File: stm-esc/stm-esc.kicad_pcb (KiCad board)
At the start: 2 copper layers, 90 x 90 mm, 48 parts, among them J1 Conn_01x06, J10 Conn_01x02, J11 AOUT, J12 Conn_01x02, J13 CONN_01X01, J14 CONN_01X01, J15 BOUT, J16 COUT, J3 Conn_01x06, J4 Conn_01x03, J5 Conn_01x02, J6 Conn_01x06, J7 Conn_01x04, J8 Conn_01x04, J9 Conn_01x06, Q1 FDMS86350, Q2 FDMS86350, Q3 FDMS86350, Q4 FDMS86350, Q5 FDMS86350, Q6 FDMS86350, U1 L7805, U2 APE8865N-33-HF-3, U3 STM32F0XX-QFP48, U4 IR2103, U5 IR2103, U6 IR2103

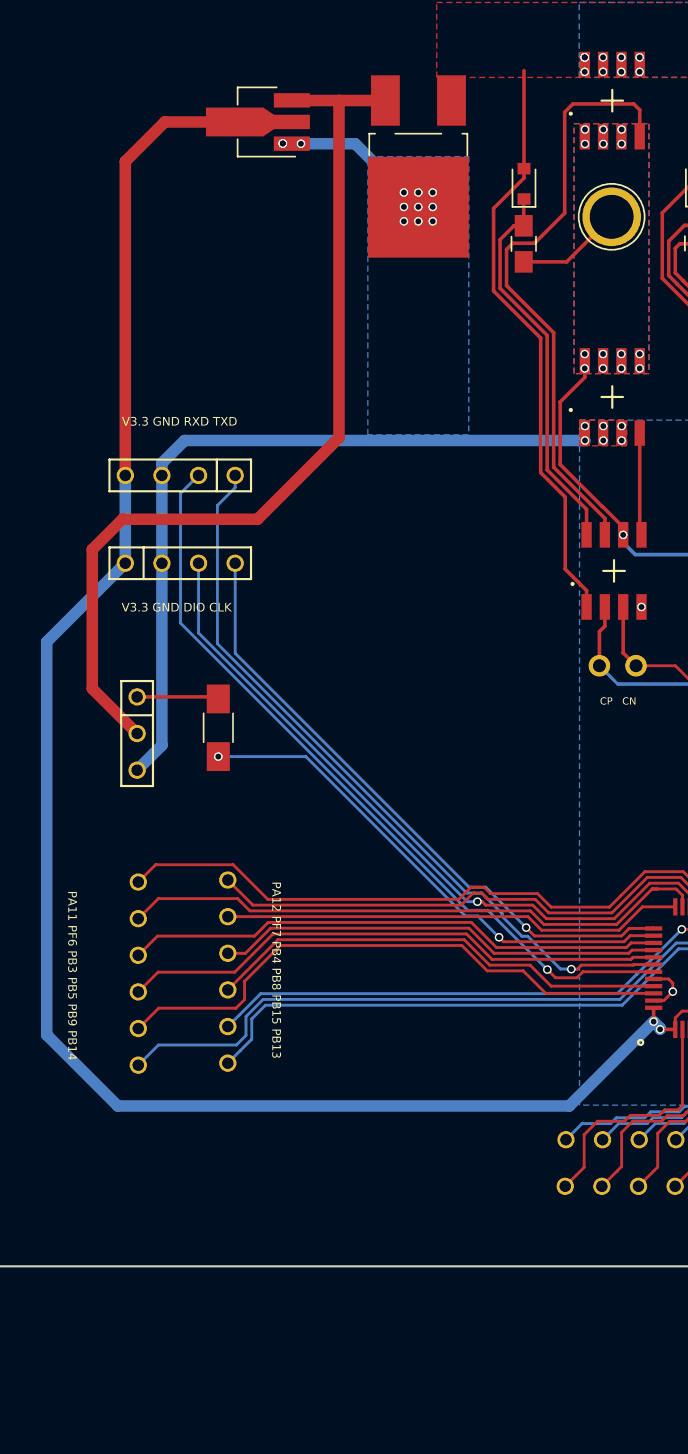
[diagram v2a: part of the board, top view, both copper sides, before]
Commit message: correct pin define for regular v3.3
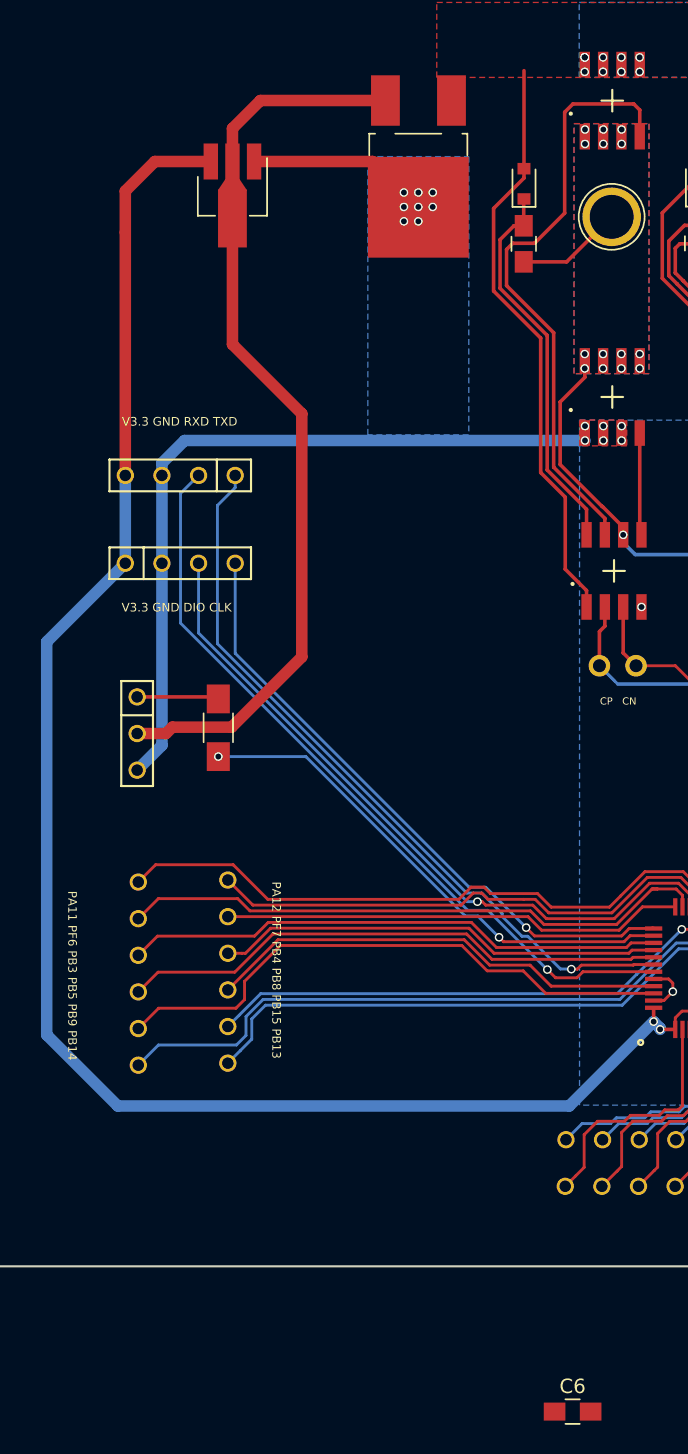
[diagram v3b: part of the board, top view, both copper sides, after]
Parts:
- added C6: C, Capacitors_SMD:C_0805_HandSoldering, F.Cu at (65.0, 120.1)
- moved U2 5.18 mm to (41.4, 35.4), turned to 270 degrees
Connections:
- U2 pad 2: +3V3 -> +5V
- U2 pad 3: +5V -> +3V3
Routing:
- net +5V: track 64.3 -> 59.7 mm
- net +3V3: track 144.6 -> 140.6 mm
- net GND: vias 38 -> 34
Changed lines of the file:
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@@
 (kicad_pcb (version 4) (host pcbnew 4.0.7)
   (general
-    (links 159)
-    (no_connects 4)
+    (links 161)
+    (no_connects 8)
     (area 19.924999 19.924999 110.075001 110.075001)
     (thickness 1.6)
     (drawings 13)
-    (tracks 799)
+    (tracks 794)
     (zones 0)
-    (modules 48)
+    (modules 49)
     (nets 58)
   )
@@
   )
   (setup
-    (last_trace_width 0.2)
+    (last_trace_width 0.8)
     (user_trace_width 0.2)
     (user_trace_width 0.8)
@@
   )
   (module TO_SOT_Packages_SMD:SOT-89-3_Handsoldering (layer F.Cu)
-    (at 43.55 30.64 180)
+    (at 41.41 35.36 270)
     (descr "SOT-89-3 Handsoldering")
     (tags "SOT-89-3 Handsoldering")
     (attr smd)
-    (fp_text reference U2 (at 0.45 -3.3 180) (layer F.SilkS) hide
-      (effects (font (size 1 1) (thickness 0.15)))
-    )
-    (fp_text value APE8865N-33-HF-3 (at 0.5 3.15 180) (layer F.Fab) hide
-      (effects (font (size 1 1) (thickness 0.15)))
-    )
-    (fp_text user %R (at 0.38 0 270) (layer F.Fab)
+    (fp_text reference U2 (at 0.45 -3.3 270) (layer F.SilkS) hide
+      (effects (font (size 1 1) (thickness 0.15)))
+    )
+    (fp_text value APE8865N-33-HF-3 (at 0.5 3.15 270) (layer F.Fab) hide
+      (effects (font (size 1 1) (thickness 0.15)))
+    )
+    (fp_text user %R (at 0.38 0 360) (layer F.Fab)
       (effects (font (size 0.6 0.6) (thickness 0.09)))
     )
@@
     (fp_line (start -0.92 2.3) (end -0.92 -1.51) (layer F.Fab) (width 0.1))
     (fp_line (start -0.13 -2.3) (end 1.68 -2.3) (layer F.Fab) (width 0.1))
-    (pad 1 smd rect (at -1.98 -1.5 90) (size 1 2.5) (layers F.Cu F.Paste F.Mask)
-      (net 1 GND))
-    (pad 2 smd rect (at -1.98 0 90) (size 1 2.5) (layers F.Cu F.Paste F.Mask)
+    (pad 1 smd rect (at -1.98 -1.5 180) (size 1 2.5) (layers F.Cu F.Paste F.Mask)
+      (net 1 GND))
+    (pad 2 smd rect (at -1.98 0 180) (size 1 2.5) (layers F.Cu F.Paste F.Mask)
+      (net 12 +5V))
+    (pad 3 smd rect (at -1.98 1.5 180) (size 1 2.5) (layers F.Cu F.Paste F.Mask)
       (net 2 +3V3))
-    (pad 3 smd rect (at -1.98 1.5 90) (size 1 2.5) (layers F.Cu F.Paste F.Mask)
+    (pad 2 smd rect (at 1.98 0 180) (size 2 4) (layers F.Cu F.Paste F.Mask)
       (net 12 +5V))
-    (pad 2 smd rect (at 1.98 0 90) (size 2 4) (layers F.Cu F.Paste F.Mask)
-      (net 2 +3V3))
-    (pad 2 smd trapezoid (at -0.37 0 270) (size 1.5 0.75) (rect_delta 0 0.5 ) (layers F.Cu F.Paste F.Mask)
-      (net 2 +3V3))
+    (pad 2 smd trapezoid (at -0.37 0) (size 1.5 0.75) (rect_delta 0 0.5 ) (layers F.Cu F.Paste F.Mask)
+      (net 12 +5V))
     (model ${KISYS3DMOD}/TO_SOT_Packages_SMD.3dshapes/SOT-89-3.wrl
       (at (xyz 0 0 0))
@@
     )
   )
+  (module Capacitors_SMD:C_0805_HandSoldering (layer F.Cu)
+    (at 65 120.075001)
+    (descr "Capacitor SMD 0805, hand soldering")
+    (tags "capacitor 0805")
+    (attr smd)
+    (fp_text reference C6 (at 0 -1.75) (layer F.SilkS)
+      (effects (font (size 1 1) (thickness 0.15)))
+    )
+    (fp_text value C (at 0 1.75) (layer F.Fab)
+      (effects (font (size 1 1) (thickness 0.15)))
+    )
+    (fp_text user %R (at 0 -1.75) (layer F.Fab)
+      (effects (font (size 1 1) (thickness 0.15)))
+    )
+    (fp_line (start -1 0.62) (end -1 -0.62) (layer F.Fab) (width 0.1))
+    (fp_line (start 1 0.62) (end -1 0.62) (layer F.Fab) (width 0.1))
+    (fp_line (start 1 -0.62) (end 1 0.62) (layer F.Fab) (width 0.1))
+    (fp_line (start -1 -0.62) (end 1 -0.62) (layer F.Fab) (width 0.1))
+    (fp_line (start 0.5 -0.85) (end -0.5 -0.85) (layer F.SilkS) (width 0.12))
+    (fp_line (start -0.5 0.85) (end 0.5 0.85) (layer F.SilkS) (width 0.12))
+    (fp_line (start -2.25 -0.88) (end 2.25 -0.88) (layer F.CrtYd) (width 0.05))
+    (fp_line (start -2.25 -0.88) (end -2.25 0.87) (layer F.CrtYd) (width 0.05))
+    (fp_line (start 2.25 0.87) (end 2.25 -0.88) (layer F.CrtYd) (width 0.05))
+    (fp_line (start 2.25 0.87) (end -2.25 0.87) (layer F.CrtYd) (width 0.05))
+    (pad 1 smd rect (at -1.25 0) (size 1.5 1.25) (layers F.Cu F.Paste F.Mask)
+      (net 1 GND))
+    (pad 2 smd rect (at 1.25 0) (size 1.5 1.25) (layers F.Cu F.Paste F.Mask)
+      (net 33 /Vsample))
+    (model Capacitors_SMD.3dshapes/C_0805.wrl
+      (at (xyz 0 0 0))
+      (scale (xyz 1 1 1))
+      (rotate (xyz 0 0 0))
+    )
+  )
   (gr_text "AP   AN" (at 91.41 70.71) (layer F.SilkS)
     (effects (font (size 0.5 0.5) (thickness 0.05)))
@@
   (gr_line (start 20 20) (end 20 110) (layer Edge.Cuts) (width 0.15))
   (gr_line (start 20 20) (end 110 20) (layer Edge.Cuts) (width 0.15))
+  (segment (start 42.91 33.38) (end 51.13 33.38) (width 0.8) (layer F.Cu) (net 1))
+  (segment (start 51.13 33.38) (end 54.3 36.55) (width 0.8) (layer F.Cu) (net 1))
   (segment (start 71.95 90.36) (end 71.95 90.95) (width 0.2) (layer F.Cu) (net 1))
   (segment (start 70.62 91.57) (end 71.33 91.57) (width 0.2) (layer F.Cu) (net 1))
@@
   (via (at 81.427514 64.272068) (size 0.6) (drill 0.4) (layers F.Cu B.Cu) (net 1))
   (via (at 69.777514 64.272068) (size 0.6) (drill 0.4) (layers F.Cu B.Cu) (net 1))
-  (segment (start 46.16 32.15) (end 49.92 32.15) (width 0.8) (layer B.Cu) (net 1))
-  (segment (start 49.92 32.15) (end 55.3 37.53) (width 0.8) (layer B.Cu) (net 1))
-  (segment (start 44.9 32.13) (end 46.14 32.13) (width 0.8) (layer B.Cu) (net 1))
-  (segment (start 46.14 32.13) (end 46.16 32.15) (width 0.8) (layer B.Cu) (net 1))
-  (via (at 46.16 32.15) (size 0.6) (drill 0.4) (layers F.Cu B.Cu) (net 1))
-  (via (at 44.9 32.13) (size 0.6) (drill 0.4) (layers F.Cu B.Cu) (net 1))
-  (via (at 44.9 32.13) (size 0.6) (drill 0.4) (layers F.Cu B.Cu) (net 1))
-  (via (at 55.3 37.53) (size 0.6) (drill 0.4) (layers F.Cu B.Cu) (net 1))
   (via (at 54.3 37.53) (size 0.6) (drill 0.4) (layers F.Cu B.Cu) (net 1))
   (via (at 53.3 37.53) (size 0.6) (drill 0.4) (layers F.Cu B.Cu) (net 1))
@@
   (via (at 67.13 51.73) (size 0.6) (drill 0.4) (layers F.Cu B.Cu) (net 1))
   (via (at 65.86 51.73) (size 0.6) (drill 0.4) (layers F.Cu B.Cu) (net 1))
+  (segment (start 33.98 55.15) (end 33.98 38.3) (width 0.8) (layer F.Cu) (net 2) (status 400000))
+  (segment (start 36.03 33.38) (end 39.91 33.38) (width 0.8) (layer F.Cu) (net 2) (status 800000))
+  (segment (start 33.98 35.43) (end 36.03 33.38) (width 0.8) (layer F.Cu) (net 2))
+  (segment (start 33.98 38.3) (end 33.98 35.43) (width 0.8) (layer F.Cu) (net 2))
   (segment (start 70.62 93.03) (end 64.77 98.88) (width 0.8) (layer B.Cu) (net 2))
   (segment (start 64.77 98.88) (end 33.46 98.88) (width 0.8) (layer B.Cu) (net 2))
@@
   (segment (start 28.53 93.95) (end 28.53 66.69) (width 0.8) (layer B.Cu) (net 2))
   (segment (start 33.98 61.24) (end 33.98 55.15) (width 0.8) (layer B.Cu) (net 2))
-  (segment (start 33.98 55.15) (end 33.98 33.38) (width 0.8) (layer F.Cu) (net 2))
-  (segment (start 33.98 33.38) (end 36.72 30.64) (width 0.8) (layer F.Cu) (net 2))
-  (segment (start 36.72 30.64) (end 41.57 30.64) (width 0.8) (layer F.Cu) (net 2))
   (segment (start 76.130001 92.759999) (end 76.130001 92.32) (width 0.2) (layer F.Cu) (net 2))
   (segment (start 76.130001 92.32) (end 76.130001 90.890001) (width 0.2) (layer F.Cu) (net 2))
@@
   (via (at 67.11 26.16) (size 0.6) (drill 0.4) (layers F.Cu B.Cu) (net 11))
   (via (at 65.84 26.16) (size 0.6) (drill 0.4) (layers F.Cu B.Cu) (net 11))
-  (segment (start 52.02 29.15) (end 48.82 29.15) (width 0.8) (layer F.Cu) (net 12))
-  (segment (start 48.82 29.15) (end 45.54 29.15) (width 0.8) (layer F.Cu) (net 12))
-  (segment (start 48.8 52.54) (end 48.8 29.17) (width 0.8) (layer F.Cu) (net 12))
-  (segment (start 48.8 29.17) (end 48.82 29.15) (width 0.8) (layer F.Cu) (net 12))
-  (segment (start 45.54 29.15) (end 45.53 29.14) (width 0.8) (layer F.Cu) (net 12))
-  (segment (start 43.15 58.19) (end 48.8 52.54) (width 0.8) (layer F.Cu) (net 12))
-  (segment (start 33.79 58.19) (end 43.15 58.19) (width 0.8) (layer F.Cu) (net 12))
-  (segment (start 31.69 60.29) (end 33.79 58.19) (width 0.8) (layer F.Cu) (net 12))
-  (segment (start 34.8 73.05) (end 31.69 69.94) (width 0.8) (layer F.Cu) (net 12))
-  (segment (start 31.69 69.94) (end 31.69 60.29) (width 0.8) (layer F.Cu) (net 12))
+  (segment (start 46.22 50.87) (end 41.41 46.06) (width 0.8) (layer F.Cu) (net 12))
+  (segment (start 41.41 46.06) (end 41.41 37.34) (width 0.8) (layer F.Cu) (net 12))
+  (segment (start 46.22 67.740002) (end 46.22 50.87) (width 0.8) (layer F.Cu) (net 12))
+  (segment (start 37.24 72.61) (end 41.350002 72.61) (width 0.8) (layer F.Cu) (net 12))
+  (segment (start 41.350002 72.61) (end 46.22 67.740002) (width 0.8) (layer F.Cu) (net 12))
+  (segment (start 36.8 73.05) (end 37.24 72.61) (width 0.8) (layer F.Cu) (net 12))
+  (segment (start 34.8 73.05) (end 36.8 73.05) (width 0.8) (layer F.Cu) (net 12))
+  (segment (start 41.41 33.38) (end 41.41 31.09) (width 0.8) (layer F.Cu) (net 12) (status 400000))
+  (segment (start 43.35 29.15) (end 52.02 29.15) (width 0.8) (layer F.Cu) (net 12) (status 800000))
+  (segment (start 41.41 31.09) (end 43.35 29.15) (width 0.8) (layer F.Cu) (net 12))
   (segment (start 91.807514 64.272068) (end 91.807514 67.407514) (width 0.25) (layer F.Cu) (net 13))
   (segment (start 91.807514 67.407514) (end 92.75 68.35) (width 0.25) (layer F.Cu) (net 13))

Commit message: working
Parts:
- removed the R2 at (98.1, 92.2)
- removed the R2 at (100.6, 92.2)
- added BT1: Battery_Cell, Battery:BatteryHolder_Keystone_103_1x20mm, F.Cu at (0.00, 0.00)
- added BZ1: Buzzer, Buzzer_Beeper:Buzzer_12x9.5RM7.6, F.Cu at (20.0, 0.00)
- added C7: Cb, Capacitor_SMD:C_0603_1608Metric_Pad1.05x0.95mm_HandSolder, F.Cu at (89.7, 40.9)
- added D4: Dc, Diode_SMD:D_0603_1608Metric_Pad1.05x0.95mm_HandSolder, F.Cu at (79.7, 38.4)
- added D5: Db, Diode_SMD:D_0603_1608Metric_Pad1.05x0.95mm_HandSolder, F.Cu at (90.6, 38.4)
- added J2: Conn_01x06, footprint:conn-6x2.54mm, F.Cu at (120.0, 20.0)
- added Q7: nfet, footprint:SOIC-8, F.Cu at (85.6, 43.4)
- added R13: 1k, Resistor_SMD:R_0603_1608Metric_Pad1.05x0.95mm_HandSolder, F.Cu at (78.9, 78.8)
- added R14: 20k, Resistor_SMD:R_0603_1608Metric_Pad1.05x0.95mm_HandSolder, F.Cu at (82.6, 82.5)
- added R15: 20k, Resistor_SMD:R_0603_1608Metric_Pad1.05x0.95mm_HandSolder, F.Cu at (82.6, 78.8)
- added R2: 1R, Resistor_SMD:R_0805_2012Metric_Pad1.15x1.40mm_HandSolder, F.Cu at (79.3, 75.2)
- C1: footprint Capacitors_SMD:C_1206_HandSoldering -> Capacitor_SMD:C_0603_1608Metric_Pad1.05x0.95mm_HandSolder
- C2: footprint Capacitors_SMD:C_1206_HandSoldering -> Capacitor_SMD:C_0805_2012Metric_Pad1.15x1.40mm_HandSolder
- C3: footprint Capacitors_SMD:C_0805_HandSoldering -> Capacitor_SMD:C_0603_1608Metric
- C4: footprint Capacitors_SMD:C_0805_HandSoldering -> Capacitor_SMD:C_0603_1608Metric_Pad1.05x0.95mm_HandSolder
- C5: value C -> Ca; footprint Capacitors_SMD:C_0805_HandSoldering -> Capacitor_SMD:C_0603_1608Metric_Pad1.05x0.95mm_HandSolder
- C6: value C -> Cc; footprint Capacitors_SMD:C_0805_HandSoldering -> Capacitor_SMD:C_0603_1608Metric_Pad1.05x0.95mm_HandSolder
- D1: footprint Diodes_SMD:D_0805 -> Diode_THT:D_5W_P10.16mm_Horizontal
- D2: value D -> LED; footprint Diodes_SMD:D_0805 -> LED_THT:LED_D4.0mm
- D3: value D -> Da; footprint Diodes_SMD:D_0805 -> Diode_SMD:D_0603_1608Metric_Pad1.05x0.95mm_HandSolder
- J1, J3: footprint my_footprint:conn-6x2.54mm -> footprint:conn-6x2.54mm
- J10: value Conn_01x02 -> Conn_01x03; footprint my_footprint:SIP-2xP2.54mm -> footprint:conn-3x2.54mm
- J11: value AOUT -> Conn_01x02; footprint Connectors:1pin -> footprint:SIP-2xP2.54mm
- J12: footprint my_footprint:SIP-2xP2.54mm -> footprint:SIP-2xP2.54mm
- J13: value CONN_01X01 -> Conn_01x02; footprint Connectors:1pin -> footprint:SIP-2xP2.54mm
- J14: value CONN_01X01 -> Conn_01x01; footprint Connectors:1pin -> footprint:HOLE-R1.5MM
- J15: value BOUT -> Conn_01x01; footprint Connectors:1pin -> footprint:HOLE-R1.5MM
- J16: value COUT -> Conn_01x01; footprint Connectors:1pin -> footprint:HOLE-R1.5MM
- J4: value Conn_01x03 -> Conn_01x06; footprint my_footprint:conn-3x2.54mm -> footprint:conn-6x2.54mm
- J5: value Conn_01x02 -> Conn_01x01; footprint my_footprint:SIP-2xP2.54mm -> Connector_Pin:Pin_D1.3mm_L10.0mm_W3.5mm_Flat
- J6: value Conn_01x06 -> Conn_01x04; footprint my_footprint:conn-6x2.54mm -> Connector_PinSocket_2.54mm:PinSocket_1x04_P2.54mm_Vertical
- J7: footprint my_footprint:conn-4x2.54mm -> Connector_PinSocket_2.54mm:PinSocket_1x04_P2.54mm_Vertical
- J8: value Conn_01x04 -> Conn_01x01; footprint my_footprint:conn-4x2.54mm -> footprint:HOLE-R1.5MM
- J9: value Conn_01x06 -> Conn_01x01; footprint my_footprint:conn-6x2.54mm -> footprint:HOLE-R1.5MM
- Q1: value FDMS86350 -> 2N7002; footprint my_footprint:SOIC-8 -> Package_TO_SOT_SMD:SOT-23
- Q2, Q3, Q4, Q5, Q6: value FDMS86350 -> nfet; footprint my_footprint:SOIC-8 -> footprint:SOIC-8
- R1: value R -> 1k; footprint Resistors_SMD:R_0805_HandSoldering -> Resistor_SMD:R_0603_1608Metric_Pad1.05x0.95mm_HandSolder
- R10, R12, R8: value 20K -> 20k; footprint Resistors_SMD:R_0603_HandSoldering -> Resistor_SMD:R_0603_1608Metric_Pad1.05x0.95mm_HandSolder
- R11, R7, R9: value 20K -> 3k; footprint Resistors_SMD:R_0603_HandSoldering -> Resistor_SMD:R_0603_1608Metric_Pad1.05x0.95mm_HandSolder
- R3: value 3K -> 1K; footprint Resistors_SMD:R_0603_HandSoldering -> Resistor_THT:R_Axial_DIN0204_L3.6mm_D1.6mm_P7.62mm_Horizontal
- R4, R5: value 3K -> 2K; footprint Resistors_SMD:R_0603_HandSoldering -> Resistor_SMD:R_0805_2012Metric_Pad1.15x1.40mm_HandSolder
- R6: value 1K -> 20k; footprint Resistors_SMD:R_0603_HandSoldering -> Resistor_SMD:R_0603_1608Metric_Pad1.05x0.95mm_HandSolder
- U1: value L7805 -> STM32F051C8Tx; footprint TO_SOT_Packages_SMD:TO-252-2_Rectifier -> Package_QFP:LQFP-48_7x7mm_P0.5mm
- U2: value APE8865N-33-HF-3 -> KA78M05_TO252; footprint TO_SOT_Packages_SMD:SOT-89-3_Handsoldering -> Package_TO_SOT_SMD:TO-252-2
- U3: value STM32F0XX-QFP48 -> REGULAR-7133-1; footprint my_footprint:QFP_48_P0.5_W0.3 -> Package_TO_SOT_SMD:SOT-89-3_Handsoldering
- U4, U5, U6: footprint my_footprint:SOIC-8 -> footprint:SOIC-8
- moved J4 136.0 mm to (160.0, 20.0), turned to 0 degrees
- moved J3 109.2 mm to (140.0, 20.0), turned to 0 degrees
- moved J1 89.1 mm to (100.3, 17.2)
- moved Q1 88.9 mm to (4.61, 50.0), turned to 0 degrees
- moved D1 86.6 mm to (0.00, 20.0), turned to 0 degrees
- moved J9 84.3 mm to (106.9, 45.9), turned to 0 degrees
- moved R1 81.0 mm to (20.0, 80.0), turned to 0 degrees
- moved C6 80.3 mm to (78.8, 40.9), turned to 180 degrees
- moved J8 78.5 mm to (106.9, 24.1)
- moved J5 73.8 mm to (0.00, 40.0)
- moved J10 60.3 mm to (93.3, 8.12)
- moved D2 55.7 mm to (20.0, 20.0), turned to 0 degrees
- moved C4 54.3 mm to (82.2, 92.7), turned to 180 degrees
- moved J6 53.9 mm to (20.0, 40.0), turned to 0 degrees
- moved U1 52.6 mm to (88.5, 73.7), turned to 0 degrees
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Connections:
- C1 pad 1: +3V3 -> GND
- C1 pad 2: GND -> /Vdda
- C2 pad 1: /RCP -> GND
- C2 pad 2: Net-(C2-Pad2) -> +3V3
- C3 pad 2: AOUT -> RCP
- C4 pad 1: Net-(C4-Pad1) -> V_SAMPLE
- C4 pad 2: BOUT -> GND
- C5 pad 2: COUT -> /bridge a/AOUT
- C6 pad 1: GND -> Net-(C6-Pad1)
- C6 pad 2: /Vsample -> /bridge c/COUT
- D1 pad 1: Net-(C3-Pad1) -> Net-(BT1-Pad1)
- D1 pad 2: VCC -> +3V3
- D2 pad 1: Net-(C4-Pad1) -> GND
- D2 pad 2: VCC -> Net-(D2-Pad2)
- J1 pad 1: /PB12 -> /PB5
- J1 pad 2: /PB11 -> /PB4
- J1 pad 3: /PB10 -> /PB3
- J1 pad 5: /PA3 -> /PC15
- J1 pad 6: /PA2 -> /PC14
- J10 pad 1: AP -> Net-(C3-Pad1)
- J10 pad 2: AN -> +5V
- J11 pad 1: AOUT -> CN
- J12 pad 1: BP -> BN
- J12 pad 2: BN -> BP
- J13 pad 1: VCC -> AN
- J14 pad 1: GND -> /bridge a/AOUT
- J15 pad 1: BOUT -> /bridge c/COUT
- J16 pad 1: COUT -> /bridge b/BOUT
- J3 pad 1: /NRST -> GND
- J3 pad 2: /PF1 -> /PA3
- J3 pad 3: /PF0 -> /PA11
- J3 pad 4: /PC15 -> /PA12
- J3 pad 5: /PC14 -> /PB15
- J3 pad 6: /PC13 -> /PB14
- J4 pad 1: Net-(C2-Pad2) -> /PB13
- J4 pad 2: +5V -> /PB12
- J4 pad 3: GND -> /PB11
- J5 pad 1: CP -> Net-(J5-Pad1)
- J6 pad 1: PB13 -> +3V3
- J6 pad 2: PB15 -> GND
- J6 pad 3: PB8 -> SWCLK
- J6 pad 4: PB4 -> SWDIO
- J7 pad 1: /TXD -> +3V3
- J7 pad 2: /RXD -> GND
- J7 pad 3: GND -> RXD
- J7 pad 4: +3V3 -> TXD
- J8 pad 1: +3V3 -> VCC
- J9 pad 1: PB14 -> GND
- Q1 pad 1: AOUT -> Net-(J5-Pad1)
- Q1 pad 2: AOUT -> GND
- Q1 pad 3: AOUT -> Net-(BZ1-Pad2)
- Q2 pad 1: GND -> /bridge a/AOUT
- Q2 pad 2: GND -> /bridge a/AOUT
- Q2 pad 3: GND -> /bridge a/AOUT
- Q2 pad 5: AOUT -> VCC
- Q2 pad 6: AOUT -> VCC
- Q2 pad 7: AOUT -> VCC
- Q2 pad 8: AOUT -> VCC
- Q3 pad 1: BOUT -> GND
- Q3 pad 2: BOUT -> GND
- Q3 pad 3: BOUT -> GND
- Q3 pad 5: VCC -> /bridge a/AOUT
- Q3 pad 6: VCC -> /bridge a/AOUT
- Q3 pad 7: VCC -> /bridge a/AOUT
- Q3 pad 8: VCC -> /bridge a/AOUT
- Q4 pad 1: GND -> /bridge c/COUT
- Q4 pad 2: GND -> /bridge c/COUT
- Q4 pad 3: GND -> /bridge c/COUT
- Q4 pad 5: BOUT -> VCC
- Q4 pad 6: BOUT -> VCC
- Q4 pad 7: BOUT -> VCC
- Q4 pad 8: BOUT -> VCC
- Q5 pad 1: COUT -> GND
- Q5 pad 2: COUT -> GND
- Q5 pad 3: COUT -> GND
- Q5 pad 5: VCC -> /bridge c/COUT
- Q5 pad 6: VCC -> /bridge c/COUT
- Q5 pad 7: VCC -> /bridge c/COUT
- Q5 pad 8: VCC -> /bridge c/COUT
- Q6 pad 1: GND -> /bridge b/BOUT
- Q6 pad 2: GND -> /bridge b/BOUT
- Q6 pad 3: GND -> /bridge b/BOUT
- Q6 pad 5: COUT -> VCC
- Q6 pad 6: COUT -> VCC
- Q6 pad 7: COUT -> VCC
- Q6 pad 8: COUT -> VCC
- R1 pad 1: /Vsample -> Net-(R1-Pad1)
- R1 pad 2: VCC -> +3V3
- R10 pad 1: Fabc -> /bridge a/AOUT
- R10 pad 2: COUT -> Fa
- R11 pad 1: Fabc -> Fa
- R11 pad 2: BOUT -> GND
- R12 pad 1: Fabc -> /bridge a/AOUT
- R12 pad 2: AOUT -> Fabc
- R3 pad 1: GND -> Net-(D2-Pad2)
- R3 pad 2: Fc -> Net-(R3-Pad2)
- R4 pad 1: GND -> VCC
- R4 pad 2: Fb -> V_SAMPLE
- R5 pad 1: GND -> V_SAMPLE
- R5 pad 2: Fa -> GND
- R6 pad 1: GND -> /bridge c/COUT
- R6 pad 2: Fabc -> Fc
- R7 pad 2: COUT -> GND
- R8 pad 1: Fb -> /bridge b/BOUT
- R8 pad 2: BOUT -> Fb
- R9 pad 1: Fa -> Fb
- R9 pad 2: AOUT -> GND
- U1 pad 1: VCC -> Net-(BT1-Pad1)
- U1 pad 2: GND -> /PC13
- U1 pad 3: +5V -> /PC14
- U2 pad 1: GND -> VCC
- U2 pad 2: +5V -> GND
- U2 pad 3: +3V3 -> +5V
- U3 pad 1: +3V3 -> GND
- U3 pad 2: /PC13 -> +5V
- U3 pad 3: /PC14 -> +3V3
- U4 pad 5: Net-(Q2-Pad4) -> Net-(Q3-Pad4)
- U4 pad 6: AOUT -> /bridge a/AOUT
- U4 pad 7: Net-(Q1-Pad4) -> Net-(Q2-Pad4)
- U4 pad 8: Net-(C3-Pad1) -> Net-(C5-Pad1)
- U5 pad 2: BP -> CP
- U5 pad 3: BN -> CN
- U5 pad 5: Net-(Q4-Pad4) -> Net-(Q5-Pad4)
- U5 pad 6: BOUT -> /bridge c/COUT
- U5 pad 7: Net-(Q3-Pad4) -> Net-(Q4-Pad4)
- U5 pad 8: Net-(C4-Pad1) -> Net-(C6-Pad1)
- U6 pad 2: CP -> BP
- U6 pad 3: CN -> BN
- U6 pad 5: Net-(Q6-Pad4) -> Net-(Q7-Pad4)
- U6 pad 6: COUT -> /bridge b/BOUT
- U6 pad 7: Net-(Q5-Pad4) -> Net-(Q6-Pad4)
- U6 pad 8: Net-(C5-Pad1) -> Net-(C7-Pad1)
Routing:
- net +3V3: track 140.6 -> 21.8 mm, vias 2 -> 0
- net COUT: track 93.3 -> 0.00 mm, vias 16 -> 0
- net /bridge c/COUT: track 0.00 -> 73.0 mm
- net BOUT: track 68.7 -> 0.00 mm, vias 16 -> 0
- net AOUT: track 63.9 -> 0.00 mm, vias 14 -> 0
- net /bridge b/BOUT: track 0.00 -> 62.7 mm
- net GND: track 97.4 -> 35.3 mm, vias 34 -> 1
- net /RXD: track 53.9 -> 0.00 mm, vias 1 -> 0
- net /bridge a/AOUT: track 0.00 -> 52.4 mm
- net /TXD: track 52.0 -> 0.00 mm, vias 1 -> 0
- net /SWDIO: track 49.3 -> 0.00 mm, vias 1 -> 0
- net PB14: track 47.9 -> 0.00 mm, vias 1 -> 0
- net +5V: track 59.7 -> 13.6 mm
- net VCC: track 188.5 -> 143.2 mm, vias 25 -> 5
- net PA11: track 44.3 -> 0.00 mm
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- added copper zone on B.Cu, net /bridge a/AOUT
- added copper zone on F.Cu, net /bridge a/AOUT
- added copper zone on B.Cu, net /bridge b/BOUT
- added copper zone on F.Cu, net /bridge b/BOUT
- added copper zone on B.Cu, net /bridge c/COUT
- added copper zone on F.Cu, net /bridge c/COUT
- removed copper zone on B.Cu, net AOUT
- removed copper zone on F.Cu, net AOUT
- removed copper zone on B.Cu, net BOUT
- removed copper zone on F.Cu, net BOUT
- removed copper zone on B.Cu, net COUT
- removed copper zone on F.Cu, net COUT
- removed copper zone on B.Cu, net VCC
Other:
- net class Default: via_dia 0.6 -> 0.8
- net class power removed
- net class power33 removed
- rule pad_to_mask_clearance: 0.2 -> 0
- rule via_min_drill: 0.3 -> 0
- rule via_min_size: 0.4 -> 0.2
- board text removed: "AP AN"
- board text removed: "BP BN"
- board text removed: "CP CN"
- board text removed: "PA11 PF6 PB3 PB5 PB9 PB14"
- board text removed: "PA12 PF7 PB4 PB8 PB15 PB13"
- board text removed: "PB12 PB11 PB10 PB2 PA3 PA2"
- board text removed: "PC12 PC14 PC15 PF0 PF1 NRST"
- board text removed: "V3.3 GND DIO CLK"
- board text removed: "V3.3 GND RXD TXD"

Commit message: 定板打样，单片机的退偶电容完整，数字电源和模拟电源隔离
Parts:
- added REF**: KiCad-Logo2_6mm_SilkScreen, Symbol:KiCad-Logo2_6mm_SilkScreen, F.Cu at (52.9, 105.5)
- J1: value Conn_01x06 -> A3 A2 B2 B10 F6 A12
- J11: value Conn_01x02 -> CP CN
- J12: value Conn_01x02 -> BP BN
- J13: value Conn_01x02 -> AP AN
- J2: value Conn_01x06 -> GND B12 B13 B14 B15 A11
- J6: value Conn_01x04 -> DIO CLK G 3.3
- J7: value Conn_01x04 -> TXD RXD G 3.3
- moved J4 137.3 mm to (32.6, 71.3), turned to 270 degrees
- moved J3 123.2 mm to (27.9, 71.2), turned to 270 degrees
- moved D2 111.7 mm to (107.0, 90.1), turned to 180 degrees
- moved BZ1 99.0 mm to (27.4, 98.7), turned to 270 degrees
- moved J7 93.3 mm to (106.4, 56.3)
- moved J6 92.1 mm to (106.4, 71.7)
- moved J1 91.2 mm to (82.0, 106.5), turned to 180 degrees
- moved J2 89.0 mm to (99.0, 106.5), turned to 180 degrees
- moved J10 83.6 mm to (23.8, 54.5), turned to 270 degrees
- moved C3 74.1 mm to (27.2, 52.0)
- moved D1 72.5 mm to (59.3, 61.8)
- moved J5 70.1 mm to (37.8, 99.0)
- moved Q1 64.8 mm to (36.8, 106.3), turned to 180 degrees
- moved R1 59.1 mm to (78.6, 72.4), turned to 180 degrees
- moved R3 52.6 mm to (101.8, 81.8), turned to 180 degrees
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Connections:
- J1 pad 1: /PB5 -> /PA12
- J1 pad 2: /PB4 -> /PF6
- J1 pad 3: /PB3 -> /PB10
- J1 pad 5: /PC15 -> /PA2
- J1 pad 6: /PC14 -> /PA3
- J2 pad 1: /PC13 -> /PA11
- J2 pad 2: /PF7 -> /PB15
- J2 pad 3: /PF6 -> /PB14
- J2 pad 4: /PF1 -> /PB13
- J2 pad 5: /PF0 -> /PB12
- J3 pad 2: /PA3 -> /PB5
- J3 pad 3: /PA11 -> /PB3
- J3 pad 4: /PA12 -> /PF7
- J3 pad 5: /PB15 -> /PC14
- J3 pad 6: /PB14 -> /PF0
- J4 pad 1: /PB13 -> /PB8
- J4 pad 2: /PB12 -> /PB9
- J4 pad 3: /PB11 -> /PB4
- J4 pad 4: /PB10 -> /PC13
- J4 pad 5: /PB9 -> /PC15
- J4 pad 6: /PB8 -> /PF1
- R3 pad 2: Net-(R3-Pad2) -> /LED
- U1 pad 12: Net-(R3-Pad2) -> /PA2
- U1 pad 22: /PB11 -> /LED
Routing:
- net Net-(BT1-Pad1): track 0.00 -> 103.2 mm, vias 0 -> 1
- net +5V: track 13.6 -> 97.9 mm
- net +3V3: track 21.8 -> 100.7 mm
- net RCP: track 0.00 -> 72.3 mm, vias 0 -> 2
- net /PF7: track 0.00 -> 68.2 mm, vias 0 -> 1
- net /PB3: track 0.00 -> 66.7 mm, vias 0 -> 1
- net /PB5: track 0.00 -> 64.6 mm, vias 0 -> 1
- net /PB4: track 0.00 -> 60.4 mm, vias 0 -> 1
- net /PF0: track 0.00 -> 60.4 mm, vias 0 -> 1
- net /PB8: track 0.00 -> 60.2 mm, vias 0 -> 1
- net /PC14: track 0.00 -> 58.9 mm, vias 0 -> 1
- net /PB9: track 0.00 -> 58.7 mm, vias 0 -> 1
- net /PF1: track 0.00 -> 56.1 mm, vias 0 -> 1
- net /PC15: track 0.00 -> 54.0 mm, vias 0 -> 1
- net /PC13: track 0.00 -> 53.3 mm, vias 0 -> 1
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- added copper zone on B.Cu, net VCC
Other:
- board text added: "B8 B9 B4 C13 C15 F1"
- board text added: "GND B5 B3 F7 C14 F0"
